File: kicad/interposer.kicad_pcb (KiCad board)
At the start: 6 copper layers, 48.4 x 48.7 mm, 46 parts, among them U1 PGA370, U2 uPGA2

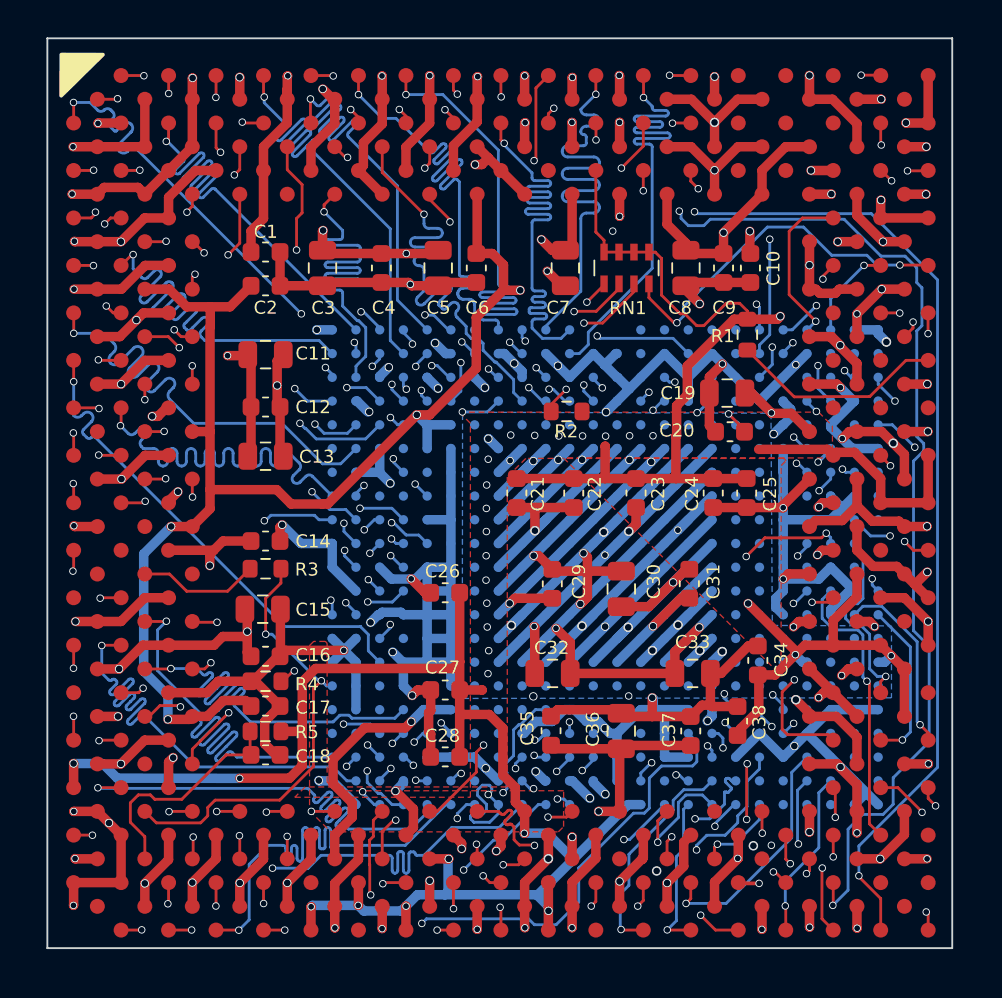
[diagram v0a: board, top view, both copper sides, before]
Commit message: Optimizations:  - remove via's out of silk screen text  - eliminate warnings  - tighter board outline
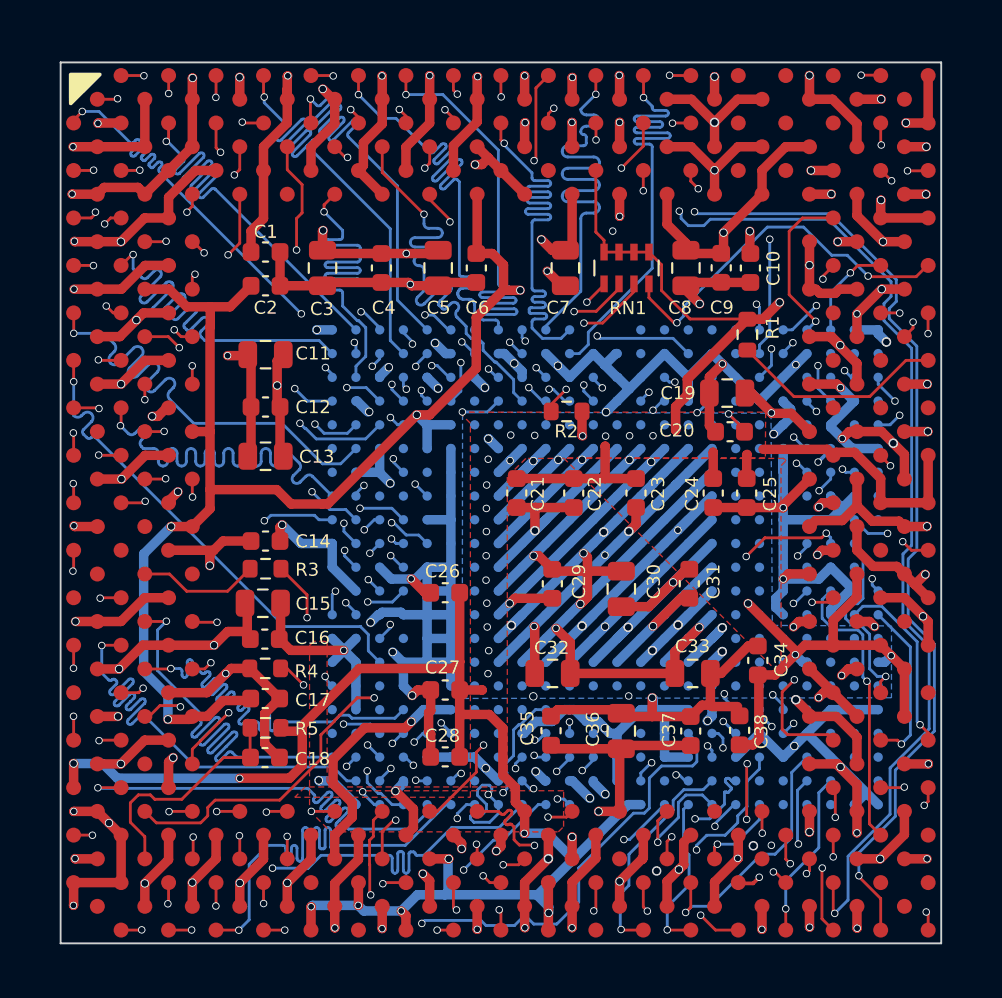
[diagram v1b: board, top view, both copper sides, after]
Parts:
- moved C16 0.92 mm to (129.1, 104.1)
- moved R4 0.69 mm to (129.1, 105.7)
- moved C38 0.51 mm to (154.5, 109.0)
- moved C17 0.40 mm to (129.1, 107.3)
- moved C15 0.32 mm to (129.0, 102.2)
- moved R5 0.19 mm to (129.1, 108.8)
- moved C18 0.15 mm to (129.1, 110.4)
- moved C9 0.13 mm to (153.5, 84.2)
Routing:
- net Net-(U1A-~{STPCLK}): track 47.2 -> 38.8 mm
- net VTT: track 180.6 -> 172.9 mm, vias 30 -> 29
- net RESET#: track 24.1 -> 29.1 mm, vias 2 -> 3
- net BCLK: track 34.1 -> 37.6 mm
- net VCORE: track 304.8 -> 303.7 mm
- net TCK: track 64.7 -> 63.7 mm
- net D5: track 26.8 -> 27.7 mm
- net Net-(U1A-~{BR0}): track 36.4 -> 37.4 mm
- net TDI: track 66.9 -> 66.1 mm
- net DBSY#: track 13.0 -> 13.7 mm
- net GND: track 467.2 -> 466.5 mm, vias 97 -> 98
- net PREQ#: track 19.5 -> 20.0 mm
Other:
- board size 48.4 x 48.7 mm -> 47.1 x 47.1 mm
- board text added: "XBOX uPGA2-P370 adapter rev. 2.1"
- board text removed: "XBOX uPGA2-P370 adapter rev. 2"

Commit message: Revision 3; much cleaner layout with traces tuned to 25mm.
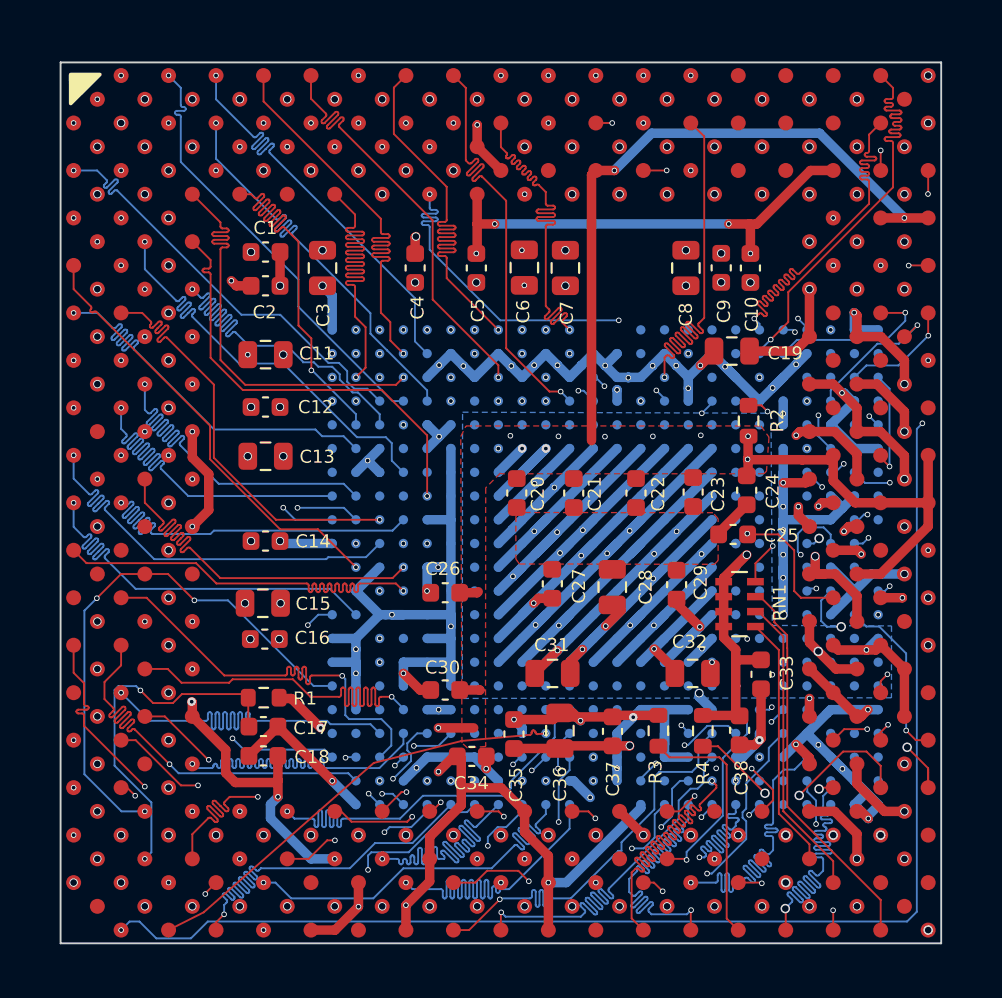
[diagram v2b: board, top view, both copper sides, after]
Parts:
- removed the R3 at (129.1, 100.3)
- moved R3 21.3 mm to (150.1, 109.0), turned to -90 degrees
- moved RN1 19.0 mm to (154.5, 102.2), turned to 0 degrees
- moved R4 18.6 mm to (152.5, 109.0), turned to -90 degrees
- moved C25 5.49 mm to (154.1, 98.5)
- moved C6 4.61 mm to (143.0, 84.2)
- moved R2 4.61 mm to (155.0, 92.4), turned to 90 degrees
- moved C37 4.19 mm to (147.7, 109.0)
- moved C36 3.28 mm to (144.9, 109.0)
- moved C18 3.07 mm to (129.0, 110.3), turned to 180 degrees
- moved C19 2.26 mm to (154.1, 88.7)
- moved C35 1.99 mm to (142.4, 109.2)
- moved C4 1.80 mm to (137.1, 84.2)
- moved C17 1.66 mm to (129.0, 108.8)
- moved R1 1.62 mm to (129.0, 107.2)
- moved C34 1.42 mm to (140.2, 110.4), turned to 0 degrees
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- renumbered C18 to C17, C17 to C18, C21 to C20, C22 to C21, C23 to C22, C24 to C23, C25 to C24, C20 to C25, C29 to C27, C30 to C28, C31 to C29, C27 to C30, C32 to C31, C33 to C32, C34 to C33, C28 to C34, C6 to C5, C5 to C6, R5 to R1, R1 to R2, R4 to R3, R2 to R4
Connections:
- U1 pad X4: Net-(U1A-RESET#) -> RESET#
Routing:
- net VCORE: track 303.7 -> 131.6 mm, vias 62 -> 95
- net GND: track 466.5 -> 295.7 mm, vias 98 -> 142
- net TCK: track 63.7 -> 16.2 mm, vias 3 -> 0
- net TDI: track 66.1 -> 20.5 mm, vias 3 -> 0
- net TMS: track 55.8 -> 13.6 mm, vias 2 -> 0
- net Net-(U1A-~{STPCLK}): track 38.8 -> 13.1 mm
- net Net-(U1A-~{BR0}): track 37.4 -> 13.2 mm, vias 2 -> 0
- net RS2#: track 4.44 -> 23.6 mm, vias 1 -> 2
- net RS0#: track 6.62 -> 23.7 mm, vias 1 -> 2
- net VTT: track 172.9 -> 156.8 mm, vias 29 -> 18
- net DRDY#: track 8.67 -> 23.7 mm
- net BP2#: track 8.71 -> 23.7 mm, vias 1 -> 2
- net ADS#: track 8.98 -> 23.7 mm
- net VREF: track 164.5 -> 150.5 mm, vias 11 -> 16
- net BCLK: track 37.6 -> 23.8 mm, vias 2 -> 3
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- added copper zone on F.Cu, net GND
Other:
- board text added: "XBOX uPGA2-P370 adapter rev. 3"
- board text removed: "XBOX uPGA2-P370 adapter rev. 2.1"

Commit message: Rev 3.1:  - change via's to 0.3mm drill/0.4mm ring for cheaper manufacturing  - add leveling 0603 resistors on backside in the corners to prevent PCB tilt during reflow
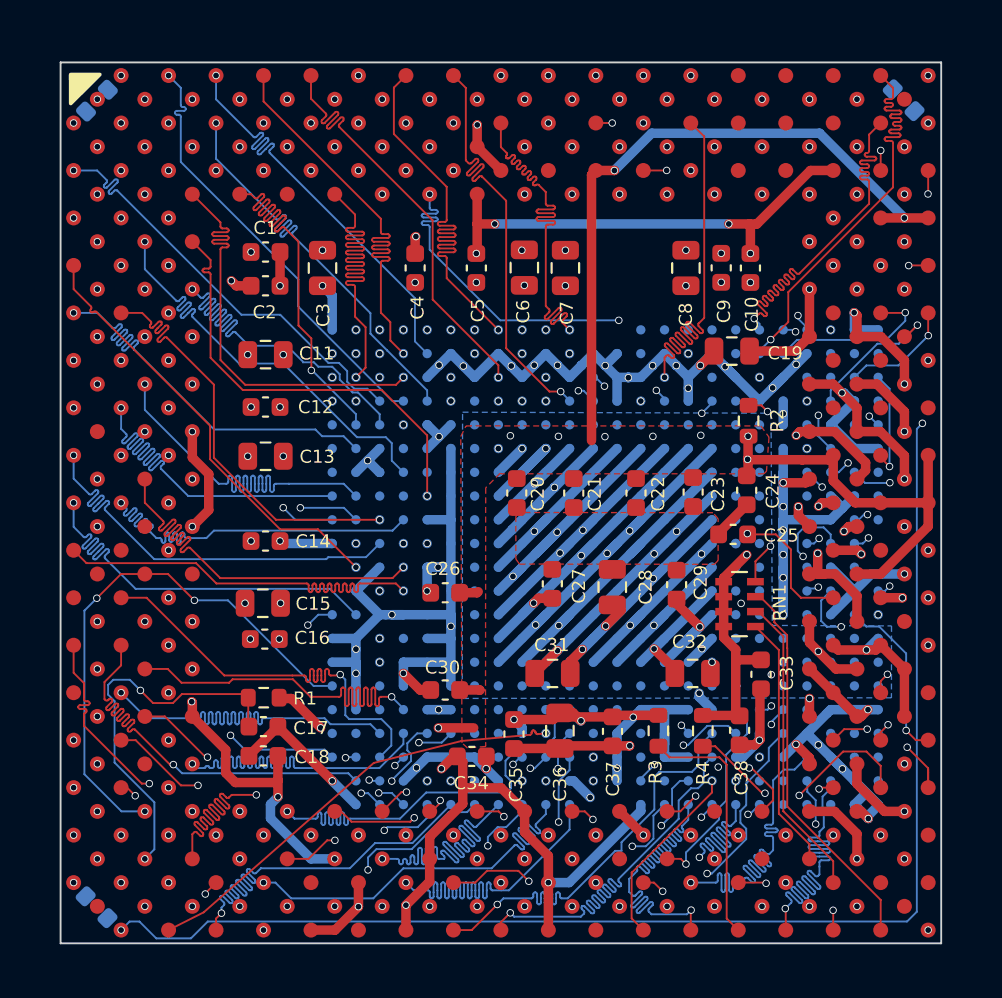
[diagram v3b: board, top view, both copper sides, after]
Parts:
- added R5: 10k, Resistor_SMD:R_0603_1608Metric, B.Cu at (163.3, 75.3)
- added R6: 10k, Resistor_SMD:R_0603_1608Metric, B.Cu at (120.1, 75.3)
- added R7: 10k, Resistor_SMD:R_0603_1608Metric, B.Cu at (120.1, 118.4)
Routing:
- net TRDY#: track 23.7 -> 10.0 mm
- net VTT: track 156.8 -> 146.5 mm
- net PREQ#: track 21.4 -> 23.9 mm
- net Net-(U1B-VTT_PWRGOOD): track 19.1 -> 20.2 mm
- net BSEL1: track 23.1 -> 23.9 mm
- net GND: track 295.7 -> 296.4 mm, vias 142 -> 141
- net SLP#: track 21.7 -> 22.3 mm
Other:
- board text added: "XBOX uPGA2-P370 adapter rev. 3.1"
- board text removed: "XBOX uPGA2-P370 adapter rev. 3"

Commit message: Revision 3.2
Implement fixes that allow interposer to be actually functional for the first time:
 - Fix uBGA495 pin P1 from VTT --> VCC since this is VCC on xbox motherboard.
 - Fix P370 pin AJ3 (RESET2#) from GND --> NC.

Furthermore, pins AL1 (reserved), AK36 (VID output), AF36 (DETECT) now left NC instead of connected to GND.

Outline slightly trimmed near bottom to provide some clearance against a cap on 1.6 motherboards.

Design specs loosened, from 4 mil tracks/4 mil clearance/0.3mm drills --> 5 mil/5 mil/0.3mm.

Board thickness recommendation is now 1.6mm instead of 1.2mm for additional rigidity.
Trace lengths now matched at 27.0mm (was 25.0mm).

Added BGA footprint indicator on front silkscreen.
Added BGA pin numbering on back silkscreen.
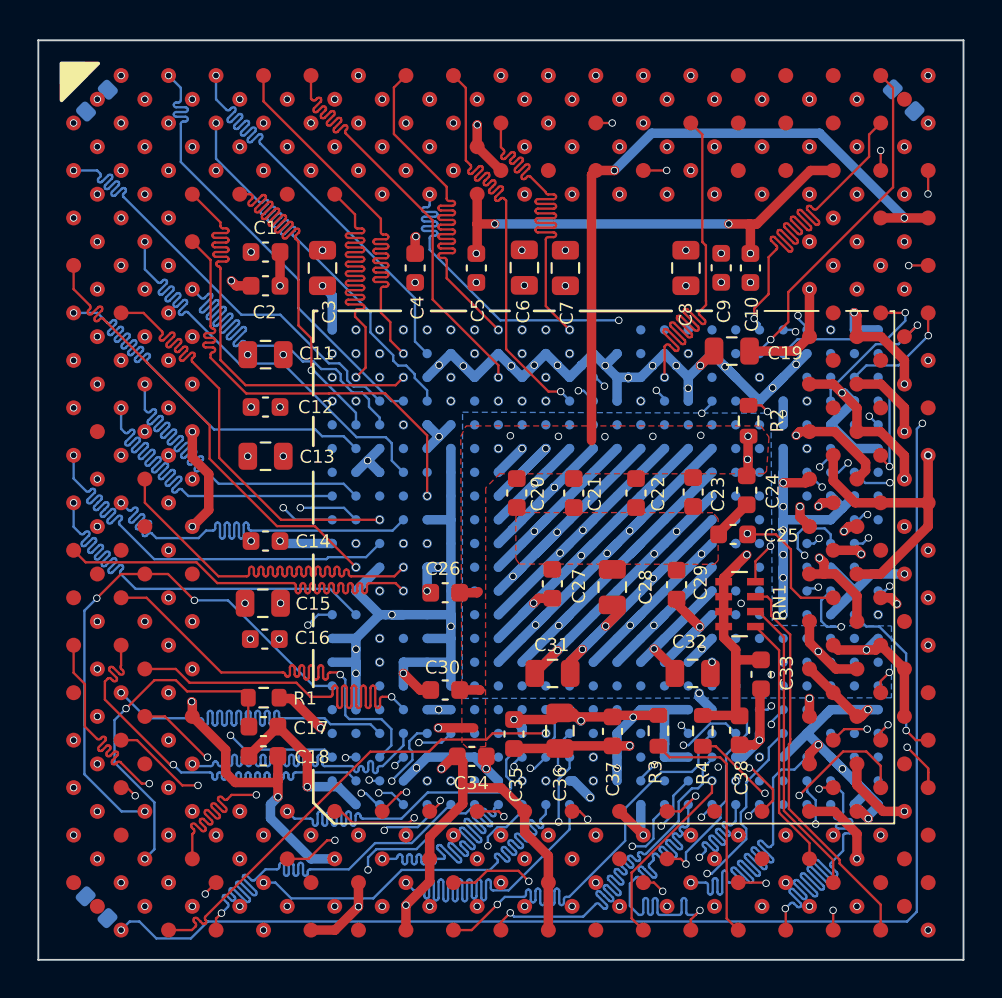
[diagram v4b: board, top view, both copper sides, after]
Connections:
- U1 pad AF36: GND -> (no net)
- U1 pad AJ3: GND -> (no net)
- U1 pad AK36: GND -> (no net)
- U1 pad AL1: GND -> (no net)
- U2 pad P1: VTT -> VCORE
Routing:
- net LOCK#: track 23.7 -> 9.90 mm
- net RS0#: track 23.7 -> 14.4 mm
- net EDGECTRLP: track 18.2 -> 25.3 mm
- net PRDY#: track 23.8 -> 18.0 mm
- net Net-(U1B-VTT_PWRGOOD): track 20.2 -> 18.2 mm
- net BPM0#: track 23.7 -> 25.3 mm
- net VCORE: track 132.0 -> 133.6 mm
- net D40: track 23.8 -> 25.4 mm
- net RS2#: track 23.6 -> 25.2 mm
- net D36: track 23.8 -> 25.4 mm
- net REQ0#: track 23.7 -> 25.3 mm
- net D55: track 23.7 -> 25.3 mm
- net A19: track 23.8 -> 25.4 mm
- net A5: track 23.7 -> 25.3 mm
- net D56: track 23.8 -> 25.4 mm
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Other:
- board size 47.1 x 47.1 mm -> 49.5 x 49.2 mm
- board text added: "21 20 19 18 17 16 15 14 13 12 11 10 9 8 7 6 5 4 3 2 1"
- board text added: "A B C D E F G H J K L M N P R T U V W Y AA AB AC AD"
- board text added: "XBOX uPGA2-P370 adapter rev. 3.2"
- board text removed: "XBOX uPGA2-P370 adapter rev. 3.1"

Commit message: Rev. 3.3, minor changes:  - Resistor network RN01 changed to 4 distinct 0603's since people continuously order an incorrect part  - Height of interposer slightly reduced by 0.3mm on both top and bottom. on top, the pins for standard mounting bracket require less trimming. On bottom there is less obstruction with C1D5 on xbox motherboard.  - Added xbox.munia.io branding on the bottom silk  - Align tool modified accordingly.
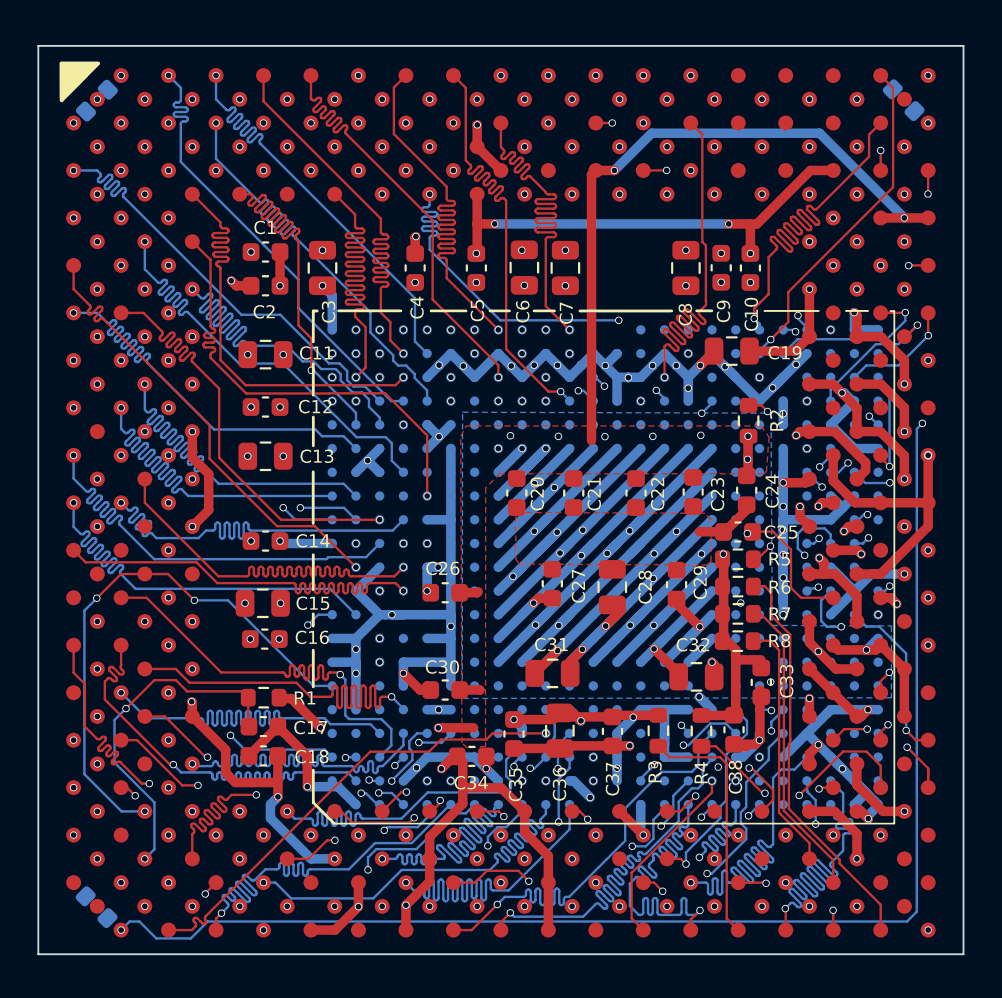
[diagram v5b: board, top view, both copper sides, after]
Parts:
- removed RN1: R_Network04, Resistor_SMD:R_Array_Concave_4x0603
- added R5: 1k, Resistor_SMD:R_0603_1608Metric, F.Cu at (154.4, 99.8)
- added R6: 1k, Resistor_SMD:R_0603_1608Metric, F.Cu at (154.4, 101.3)
- added R7: 1k, Resistor_SMD:R_0603_1608Metric, F.Cu at (154.4, 102.7)
- added R8: 1k, Resistor_SMD:R_0603_1608Metric, F.Cu at (154.4, 104.2)
- moved C33 0.43 mm to (155.7, 106.4)
- moved C38 0.30 mm to (154.2, 108.9)
- moved C25 0.29 mm to (154.4, 98.4)
- moved C32 0.27 mm to (152.2, 106.1)
- moved R4 0.07 mm to (152.4, 109.0)
- renumbered R5 to R101, R6 to R102, R7 to R103
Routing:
- net GND: track 296.8 -> 298.2 mm
- net PREQ#: track 25.5 -> 24.4 mm
- net VCORE: track 133.6 -> 134.5 mm
- net TDI: track 21.0 -> 21.6 mm
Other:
- board size 49.5 x 49.2 mm -> 49.5 x 48.6 mm
- board text added: "XBOX uPGA2-P370 adapter rev. 3.3"
- board text added: "http://xbox.munia.io"
- board text removed: "XBOX uPGA2-P370 adapter rev. 3.2"
